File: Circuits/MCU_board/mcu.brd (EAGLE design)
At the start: 100 x 80 mm, 39 parts, among them U1 TCA9548APWR, U2 USBLC6-2P6, U3 LD39050PU33R, U4 LSM9DS1, U5 STM32L452RECT6

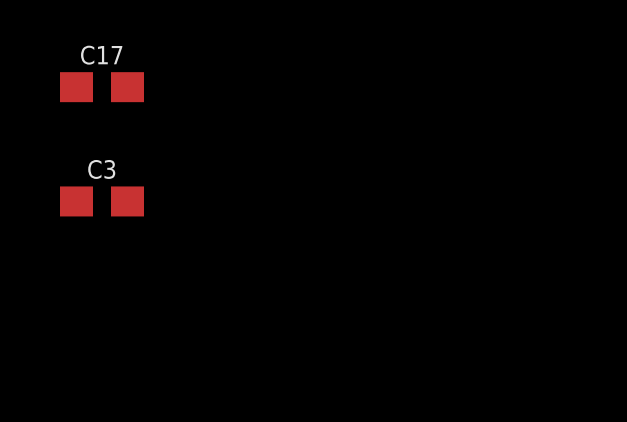
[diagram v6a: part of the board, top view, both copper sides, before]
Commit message: Added LDO part in schematic
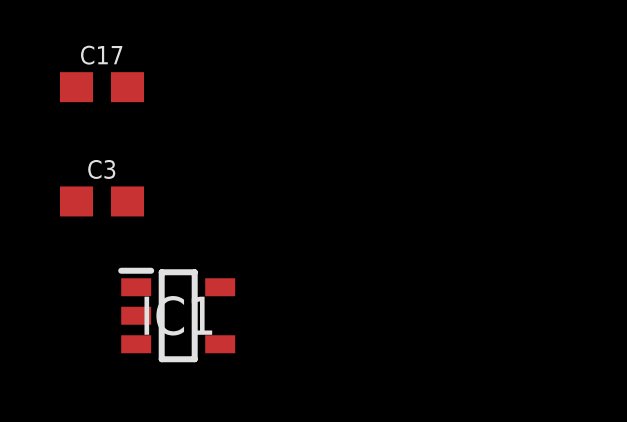
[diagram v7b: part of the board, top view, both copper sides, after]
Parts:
- added IC1: RP111N331B-TR-FE, SamacSys_Parts:SOT95P280X120-5N
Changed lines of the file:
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@@
 <?xml version="1.0" encoding="utf-8"?>
 <!DOCTYPE eagle SYSTEM "eagle.dtd">
-<eagle version="9.3.2">
+<eagle version="9.4.2">
 <drawing>
 <settings>
@@
 <attribute name="MEM" value="" x="0" y="0" size="1.778" layer="27" display="off"/>
 <attribute name="MFPN" value="STM32L476RCT6" x="0" y="0" size="1.778" layer="27" display="off"/>
+<attribute name="NAME" x="-24.52" y="13.12" size="1.016" layer="25" font="vector" ratio="18" align="bottom-right"/>
 <attribute name="NAME" x="-20.32" y="7.62" size="2" layer="151" ratio="10" align="center"/>
-<attribute name="NAME" x="-24.52" y="13.12" size="1.016" layer="25" font="vector" ratio="18" align="bottom-right"/>
 <attribute name="PARTNO" value="" x="0" y="0" size="1.778" layer="27" display="off"/>
 <attribute name="STATUS" value="" x="0" y="0" size="1.778" layer="27" display="off"/>
@@
 <attribute name="VALUE" x="-48.26" y="-127.762" size="0.6096" layer="27" font="vector" ratio="20" align="top-center"/>
 </element>
+<element name="IC1" library="SamacSys_Parts" package="SOT95P280X120-5N" value="RP111N331B-TR-FE" x="-45.72" y="-130.81" smashed="yes">
+<attribute name="DESCRIPTION" value="LDO Voltage Regulators Low voltage Fast response Regulator" x="-45.72" y="-130.81" size="1.778" layer="27" display="off"/>
+<attribute name="HEIGHT" value="1.2mm" x="-45.72" y="-130.81" size="1.778" layer="27" display="off"/>
+<attribute name="MANUFACTURER_NAME" value="Ricoh Electronic Devices Company" x="-45.72" y="-130.81" size="1.778" layer="27" display="off"/>
+<attribute name="MANUFACTURER_PART_NUMBER" value="RP111N331B-TR-FE" x="-45.72" y="-130.81" size="1.778" layer="27" display="off"/>
+<attribute name="MOUSER_PART_NUMBER" value="" x="-45.72" y="-130.81" size="1.778" layer="27" display="off"/>
+<attribute name="MOUSER_PRICE-STOCK" value="" x="-45.72" y="-130.81" size="1.778" layer="27" display="off"/>
+<attribute name="NAME" x="-45.72" y="-130.81" size="1.27" layer="25" align="center"/>
+<attribute name="RS_PART_NUMBER" value="" x="-45.72" y="-130.81" size="1.778" layer="27" display="off"/>
+<attribute name="RS_PRICE-STOCK" value="" x="-45.72" y="-130.81" size="1.778" layer="27" display="off"/>
+<attribute name="VALUE" x="-44.45" y="-130.81" size="1.27" layer="27" align="center"/>
+</element>
 </elements>

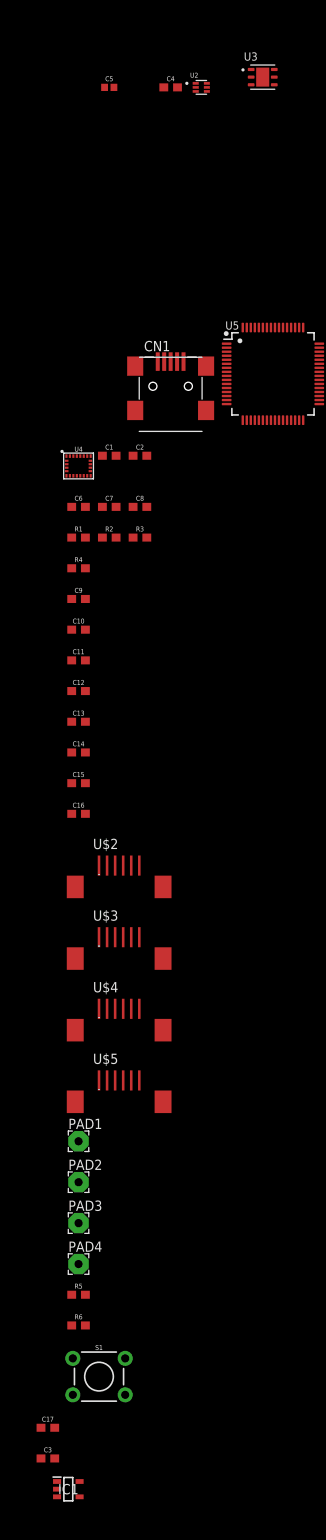
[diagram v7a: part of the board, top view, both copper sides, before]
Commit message: Added LDO and fixed TVS diode connection
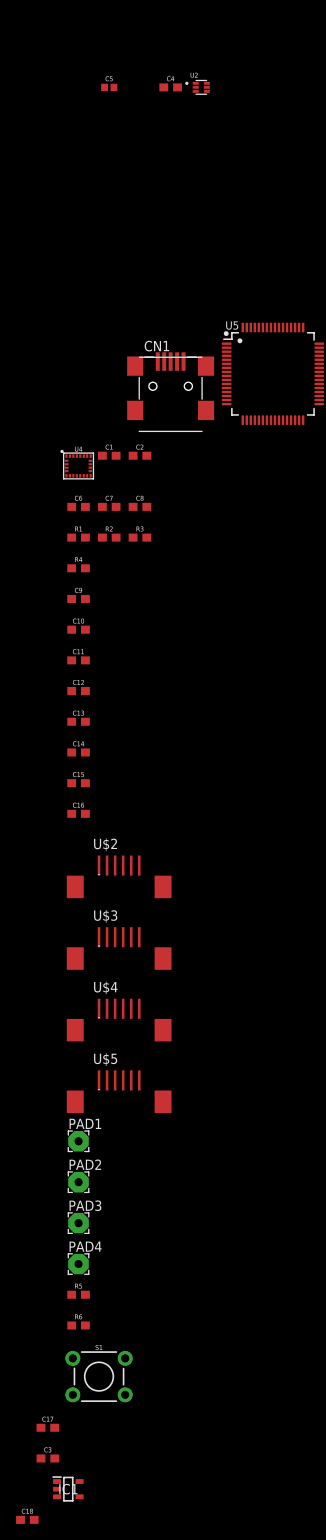
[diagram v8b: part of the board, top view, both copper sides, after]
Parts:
- removed U3: LD39050PU33R, LD39050PU33R:SON95P300X300X100-7N
- added C18: 0.1uF, SparkFun-Capacitors:0603
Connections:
- removed net N$3: C5.1, CN1.VBUS, U3.6
- new net VBUS: C18.1, C5.1, CN1.VBUS, IC1.1, IC1.3, U2.5
- net GND: now also C18.2, IC1.2; no longer U3.2, U3.7
- net VCC: no longer U2.5, U3.1
- net VDD: now also IC1.4, IC1.5; no longer U3.4
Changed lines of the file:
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@@
 <attribute name="VALUE" x="-30.51191875" y="41.37735" size="0.6105" layer="27"/>
-</element>
-<element name="U3" library="LD39050PU33R" package="SON95P300X300X100-7N" value="LD39050PU33R" x="-21.59" y="44.45" smashed="yes">
-<attribute name="AVAILABILITY" value="Unavailable" x="0" y="0" size="1.778" layer="27" display="off"/>
-<attribute name="DESCRIPTION" value=" LD39050 Series 500 mA 3.3 V Fixed Low Noise LDO Voltage Regulator - DFN-6 " x="0" y="0" size="1.778" layer="27" display="off"/>
-<attribute name="MF" value="STMicroelectronics" x="0" y="0" size="1.778" layer="27" display="off"/>
-<attribute name="MP" value="LD39050PU33R" x="0" y="0" size="1.778" layer="27" display="off"/>
-<attribute name="NAME" x="-23.93541875" y="46.502259375" size="1.016" layer="25"/>
-<attribute name="PACKAGE" value="DFN-6 STMicroelectronics" x="0" y="0" size="1.778" layer="27" display="off"/>
-<attribute name="PRICE" value="None" x="0" y="0" size="1.778" layer="27" display="off"/>
-<attribute name="VALUE" x="-23.91373125" y="41.661509375" size="1.016" layer="27"/>
 </element>
 <element name="U5" library="STM32" package="LQFP-64" value="STM32L452RECT6" x="-20.32" y="7.62" smashed="yes">
@@
 <attribute name="MEM" value="" x="0" y="0" size="1.778" layer="27" display="off"/>
 <attribute name="MFPN" value="STM32L476RCT6" x="0" y="0" size="1.778" layer="27" display="off"/>
+<attribute name="NAME" x="-20.32" y="7.62" size="2" layer="151" ratio="10" align="center"/>
 <attribute name="NAME" x="-24.52" y="13.12" size="1.016" layer="25" font="vector" ratio="18" align="bottom-right"/>
-<attribute name="NAME" x="-20.32" y="7.62" size="2" layer="151" ratio="10" align="center"/>
 <attribute name="PARTNO" value="" x="0" y="0" size="1.778" layer="27" display="off"/>
 <attribute name="STATUS" value="" x="0" y="0" size="1.778" layer="27" display="off"/>
@@
 <attribute name="VALUE" x="-44.45" y="-130.81" size="1.27" layer="27" align="center"/>
 </element>
+<element name="C18" library="SparkFun-Capacitors" package="0603" value="0.1uF" x="-50.8" y="-134.62" smashed="yes">
+<attribute name="NAME" x="-50.8" y="-133.858" size="0.6096" layer="25" font="vector" ratio="20" align="bottom-center"/>
+<attribute name="PROD_ID" value="CAP-00810" x="-50.8" y="-134.62" size="1.778" layer="27" display="off"/>
+<attribute name="VALUE" x="-50.8" y="-135.382" size="0.6096" layer="27" font="vector" ratio="20" align="top-center"/>
+</element>
 </elements>
 <signals>
@@
 </signal>
 <signal name="VCC">
-<contactref element="U2" pad="5"/>
-<contactref element="U3" pad="1"/>
 <contactref element="U4" pad="23"/>
 <contactref element="U4" pad="22"/>
@@
 <wire x1="-44.665" y1="-2.585" x2="-45.095" y2="-2.585" width="0" layer="19" extent="1-1"/>
 <wire x1="-37.68" y1="-2.54" x2="-37.68" y2="-8.89" width="0" layer="19" extent="1-1"/>
-<wire x1="-28.52" y1="43.18" x2="-37.68" y2="-2.54" width="0" layer="19" extent="1-1"/>
-<wire x1="-23.025" y1="45.4" x2="-28.52" y2="43.18" width="0" layer="19" extent="1-1"/>
 </signal>
 <signal name="GND">
@@
 <contactref element="U1" pad="2"/>
 <contactref element="U1" pad="21"/>
-<contactref element="U2" pad="2"/>
 <contactref element="CN1" pad="GND"/>
 <contactref element="CN1" pad="ID"/>
-<contactref element="U3" pad="2"/>
-<contactref element="U3" pad="7"/>
-<contactref element="C5" pad="2"/>
 <contactref element="C7" pad="2"/>
 <contactref element="C1" pad="2"/>
@@
 <contactref element="C17" pad="2"/>
 <contactref element="C3" pad="2"/>
+<contactref element="C5" pad="2"/>
+<contactref element="IC1" pad="2"/>
+<contactref element="U2" pad="2"/>
+<contactref element="C18" pad="2"/>
+<wire x1="-47.12" y1="-130.81" x2="-49.95" y2="-134.62" width="0" layer="19" extent="1-1"/>
+<wire x1="-47.41" y1="-127" x2="-47.12" y2="-130.81" width="0" layer="19" extent="1-1"/>
 <wire x1="-47.41" y1="-123.19" x2="-47.41" y2="-127" width="0" layer="19" extent="1-1"/>
 <wire x1="-45.1612" y1="-114.5794" x2="-47.41" y2="-123.19" width="0" layer="19" extent="1-1"/>
@@
 <wire x1="-33.87" y1="43.18" x2="-29.9" y2="43.18" width="0" layer="19" extent="1-1"/>
 <wire x1="-40.06" y1="43.18" x2="-33.87" y2="43.18" width="0" layer="19" extent="1-1"/>
-<wire x1="-23.025" y1="44.45" x2="-29.9" y2="43.18" width="0" layer="19" extent="1-1"/>
-<wire x1="-21.59" y1="44.45" x2="-23.025" y2="44.45" width="0" layer="19" extent="1-1"/>
 <wire x1="31.985" y1="51.6922" x2="13.43" y2="13.9" width="0" layer="19" extent="1-1"/>
 <wire x1="32.635" y1="51.6922" x2="31.985" y2="51.6922" width="0" layer="19" extent="1-1"/>
@@
 <contactref element="U1" pad="24"/>
 <contactref element="C4" pad="2"/>
-<contactref element="U3" pad="4"/>
 <contactref element="C10" pad="1"/>
 <contactref element="C9" pad="1"/>
@@
 <contactref element="PAD3" pad="1"/>
 <contactref element="C3" pad="1"/>
+<contactref element="IC1" pad="5"/>
+<contactref element="IC1" pad="4"/>
+<wire x1="-44.32" y1="-129.86" x2="-49.11" y2="-127" width="0" layer="19" extent="1-1"/>
+<wire x1="-44.32" y1="-131.76" x2="-44.32" y2="-129.86" width="0" layer="19" extent="1-1"/>
 <wire x1="-44.45" y1="-97.79" x2="-49.11" y2="-127" width="0" layer="19" extent="1-1"/>
 <wire x1="-38.91" y1="-80.08" x2="-44.45" y2="-97.79" width="0" layer="19" extent="1-1"/>
@@
 <wire x1="-24.07" y1="13.37" x2="-14.57" y2="11.37" width="0" layer="19" extent="1-1"/>
 <wire x1="14.43" y1="13.9" x2="-14.57" y2="11.37" width="0" layer="19" extent="1-1"/>
-<wire x1="-20.155" y1="43.5" x2="-24.07" y2="13.37" width="0" layer="19" extent="1-1"/>
-<wire x1="-32.17" y1="43.18" x2="-20.155" y2="43.5" width="0" layer="19" extent="1-1"/>
+<wire x1="-32.17" y1="43.18" x2="-24.07" y2="13.37" width="0" layer="19" extent="1-1"/>
 <wire x1="31.985" y1="57.5278" x2="14.43" y2="13.9" width="0" layer="19" extent="1-1"/>
 </signal>
@@
 <wire x1="-28.52" y1="42.68" x2="-33.82" y2="9.144" width="0" layer="19" extent="1-1"/>
 </signal>
-<signal name="N$3">
-<contactref element="U3" pad="6"/>
+<signal name="VBUS">
+<contactref element="CN1" pad="VBUS"/>
+<contactref element="IC1" pad="1"/>
+<contactref element="IC1" pad="3"/>
 <contactref element="C5" pad="1"/>
-<contactref element="CN1" pad="VBUS"/>
-<wire x1="-41.22" y1="43.18" x2="-20.155" y2="45.4" width="0" layer="19" extent="1-1"/>
-<wire x1="-34.62" y1="9.144" x2="-41.22" y2="43.18" width="0" layer="19" extent="1-1"/>
+<contactref element="U2" pad="5"/>
+<contactref element="C18" pad="1"/>
+<wire x1="-47.12" y1="-131.76" x2="-51.65" y2="-134.62" width="0" layer="19" extent="1-1"/>
+<wire x1="-47.12" y1="-129.86" x2="-47.12" y2="-131.76" width="0" layer="19" extent="1-1"/>
+<wire x1="-34.62" y1="9.144" x2="-47.12" y2="-129.86" width="0" layer="19" extent="1-1"/>
+<wire x1="-28.52" y1="43.18" x2="-34.62" y2="9.144" width="0" layer="19" extent="1-1"/>
+<wire x1="-41.22" y1="43.18" x2="-28.52" y2="43.18" width="0" layer="19" extent="1-1"/>
 </signal>
 <signal name="SCL7">
